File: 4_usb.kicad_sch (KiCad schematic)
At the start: 8 parts, among them J2 USB_C_Receptacle, U1 USBLC6-2SC6

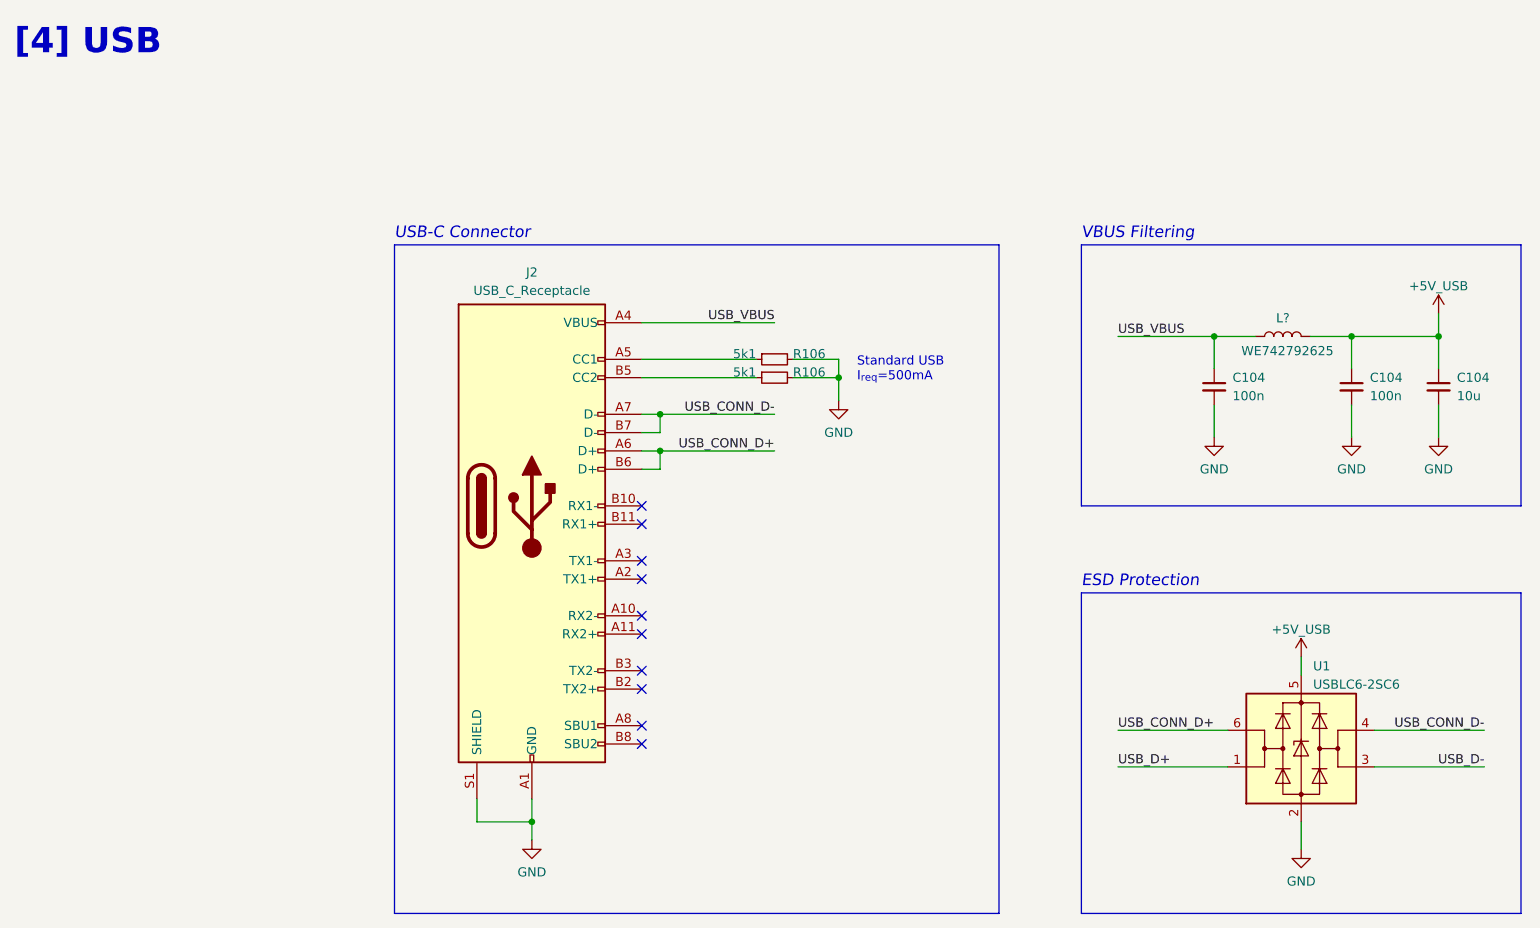
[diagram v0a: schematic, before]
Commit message: chore: updated links and footprints
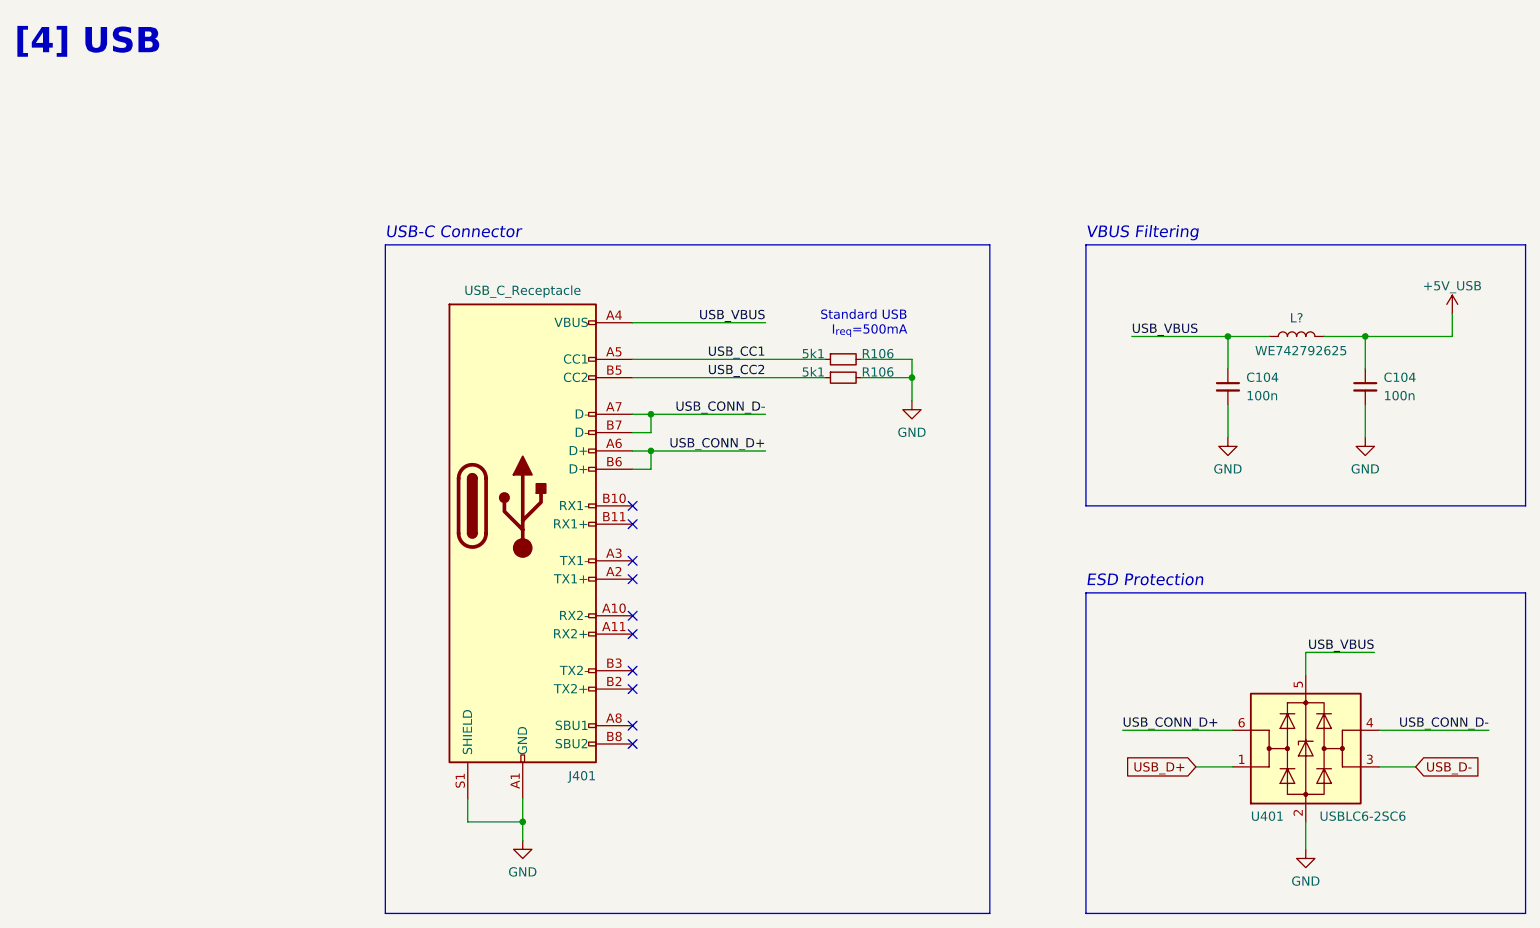
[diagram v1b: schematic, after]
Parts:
- removed C104: 10u, symbol Device:C_Small
- C104: footprint (none) -> Capacitor_SMD:C_0603_1608Metric_Pad1.08x0.95mm_HandSolder
- J401: renamed from J2; footprint (none) -> Connector_USB:USB_C_Receptacle_GCT_USB4105-xx-A_16P_TopMnt_Horizontal; Link (none) -> https://www.digikey.de/de/products/detail/gct/USB4105-GF-A/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
- L?: footprint (none) -> Inductor_SMD:L_0603_1608Metric_Pad1.05x0.95mm_HandSolder
- R106: footprint (none) -> Resistor_SMD:R_0402_1005Metric_Pad0.72x0.64mm_HandSolder
- U401: renamed from U1; Link (none) -> https://www.digikey.de/en/products/detail/stmicroelectronic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
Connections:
- net +5V: no longer U401.5 (VBUS)
- net USB_VBUS: now also U401.5 (VBUS)
- net USB_CC1: now reaches J401.A5 (CC1), R106.1
- net USB_CC2: now reaches J401.B5 (CC2), R106.1
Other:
- moved on the sheet: C104, J401, L?, R106, U401

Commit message: feat: LED routing, encoder interface, footprint updates
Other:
- title: USB [4] -> USB
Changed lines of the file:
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@@
   (paper "A4")
   (title_block
-    (title "USB [4]")
-    (date "2023-11-18")
+    (title "USB")
+    (date "2023-11-25")
     (rev "1.0")
   )

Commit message: feat: footprint assignment, circuit check and routing kickoff
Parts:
- C104: footprint Capacitor_SMD:C_0603_1608Metric_Pad1.08x0.95mm_HandSolder -> Capacitor_SMD:C_0402_1005Metric_Pad0.74x0.62mm_HandSolder
- L?: Link (none) -> https://www.digikey.de/en/products/detail/w%C3%BCrth-elektr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
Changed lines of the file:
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@@
   (title_block
     (title "USB")
-    (date "2023-11-25")
+    (date "2023-11-26")
     (rev "1.0")
   )
@@
       (effects (font (size 1.27 1.27)) hide)
     )
+    (property "Link" "https://www.digikey.de/en/products/detail/w%C3%BCrth-elektronik/742792625/4310426" (at 196.215 64.135 0)
+      (effects (font (size 1.27 1.27)) hide)
+    )
     (pin "1")
     (pin "2")
@@
       (effects (font (size 1.27 1.27)) (justify left))
     )
-    (property "Footprint" "Capacitor_SMD:C_0603_1608Metric_Pad1.08x0.95mm_HandSolder" (at 186.69 71.12 0)
+    (property "Footprint" "Capacitor_SMD:C_0402_1005Metric_Pad0.74x0.62mm_HandSolder" (at 186.69 71.12 0)
       (effects (font (size 1.27 1.27)) hide)
     )
@@
       (effects (font (size 1.27 1.27)) (justify left))
     )
-    (property "Footprint" "Capacitor_SMD:C_0603_1608Metric_Pad1.08x0.95mm_HandSolder" (at 205.74 71.12 0)
-      (effects (font (size 1.27 1.27)) hide)
-    )
+    (property "Footprint" "Capacitor_SMD:C_0402_1005Metric_Pad0.74x0.62mm_HandSolder" (at 205.74 71.12 0)
+      (effects (font (size 1.27 1.27)) hide)
+    )

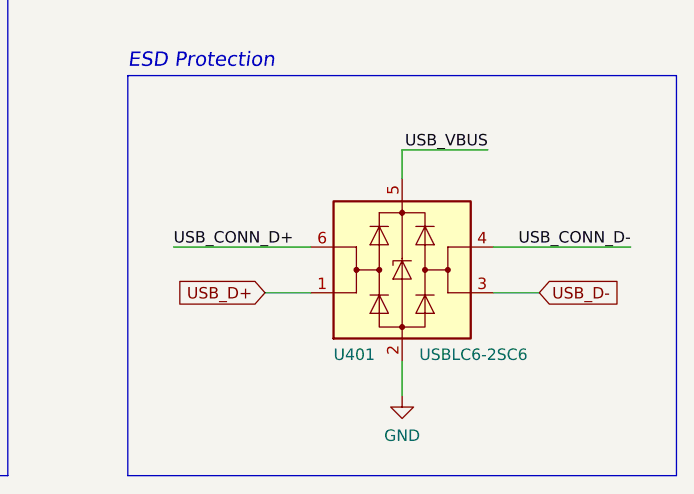
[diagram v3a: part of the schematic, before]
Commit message: feat: single phase, HSE, CAN routing and general layout
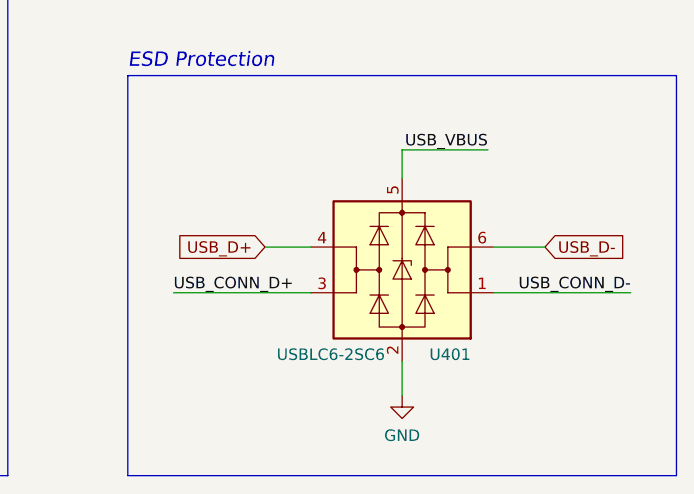
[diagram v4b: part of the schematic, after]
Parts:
- J401: footprint Connector_USB:USB_C_Receptacle_GCT_USB4105-xx-A_16P_TopMnt_Horizontal -> Connector_USB:USB_C_Receptacle_XKB_U262-16XN-4BVC11
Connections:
- net USB_CONN_D+: now also U401.3 (I/O2); no longer U401.6 (I/O1)
- net USB_CONN_D-: now also U401.1 (I/O1); no longer U401.4 (I/O2)
- net USB_D+: now also U401.4 (I/O2); no longer U401.1 (I/O1)
- net USB_D-: now also U401.6 (I/O1); no longer U401.3 (I/O2)
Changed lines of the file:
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@@
+    (stroke (width 0) (type default))
+  )
+  (wire (pts (xy 182.245 118.745) (xy 187.325 118.745))
     (stroke (width 0) (type default))
   )
@@
     (stroke (width 0) (type default))
   )
-  (wire (pts (xy 207.645 123.825) (xy 212.725 123.825))
+  (wire (pts (xy 207.645 123.825) (xy 222.885 123.825))
     (stroke (width 0) (type default))
   )
@@
     (stroke (width 0) (type default))
   )
+  (wire (pts (xy 207.645 118.745) (xy 213.36 118.745))
+    (stroke (width 0) (type default))
+  )
   (wire (pts (xy 104.14 74.93) (xy 106.68 74.93))
     (stroke (width 0) (type default))
@@
     (stroke (width 0) (type default))
   )
-  (wire (pts (xy 207.645 118.745) (xy 222.885 118.745))
-    (stroke (width 0) (type default))
-  )
   (wire (pts (xy 173.355 64.135) (xy 186.69 64.135))
     (stroke (width 0) (type default))
@@
     (stroke (width 0) (type default))
   )
-  (wire (pts (xy 172.085 118.745) (xy 187.325 118.745))
-    (stroke (width 0) (type default))
-  )
-  (wire (pts (xy 182.245 123.825) (xy 187.325 123.825))
+  (wire (pts (xy 172.085 123.825) (xy 187.325 123.825))
     (stroke (width 0) (type default))
   )
@@
     (effects (font (size 3.5 3.5) (thickness 0.8) bold) (justify left bottom))
   )
+  (label "USB_CONN_D-" (at 222.885 123.825 180) (fields_autoplaced)
+    (effects (font (size 1.27 1.27)) (justify right bottom))
+  )
   (label "USB_VBUS" (at 173.355 64.135 0) (fields_autoplaced)
     (effects (font (size 1.27 1.27)) (justify left bottom))
@@
     (effects (font (size 1.27 1.27)) (justify right bottom))
   )
-  (label "USB_CONN_D+" (at 172.085 118.745 0) (fields_autoplaced)
+  (label "USB_VBUS" (at 122.555 62.23 180) (fields_autoplaced)
+    (effects (font (size 1.27 1.27)) (justify right bottom))
+  )
+  (label "USB_CONN_D+" (at 172.085 123.825 0) (fields_autoplaced)
     (effects (font (size 1.27 1.27)) (justify left bottom))
   )
-  (label "USB_VBUS" (at 122.555 62.23 180) (fields_autoplaced)
-    (effects (font (size 1.27 1.27)) (justify right bottom))
-  )
   (label "USB_CC1" (at 122.555 67.31 180) (fields_autoplaced)
     (effects (font (size 1.27 1.27)) (justify right bottom))
   )
-  (label "USB_CONN_D-" (at 222.885 118.745 180) (fields_autoplaced)
-    (effects (font (size 1.27 1.27)) (justify right bottom))
-  )
   (label "USB_CONN_D-" (at 122.555 74.93 180) (fields_autoplaced)
     (effects (font (size 1.27 1.27)) (justify right bottom))
@@
     (effects (font (size 1.27 1.27)) (justify right bottom))
   )
-  (global_label "USB_D+" (shape input) (at 182.245 123.825 180) (fields_autoplaced)
+  (global_label "USB_D-" (shape input) (at 213.36 118.745 0) (fields_autoplaced)
+    (effects (font (size 1.27 1.27)) (justify left))
+    (property "Intersheetrefs" "${INTERSHEET_REFS}" (at 223.8858 118.745 0)
+      (effects (font (size 1.27 1.27)) (justify left) hide)
+    )
+  )
+  (global_label "USB_D+" (shape input) (at 182.245 118.745 180) (fields_autoplaced)
     (effects (font (size 1.27 1.27)) (justify right))
-    (property "Intersheetrefs" "${INTERSHEET_REFS}" (at 171.7192 123.825 0)
+    (property "Intersheetrefs" "${INTERSHEET_REFS}" (at 171.7192 118.745 0)
       (effects (font (size 1.27 1.27)) (justify right) hide)
     )
   )
-  (global_label "USB_D-" (shape input) (at 212.725 123.825 0) (fields_autoplaced)
-    (effects (font (size 1.27 1.27)) (justify left))
-    (property "Intersheetrefs" "${INTERSHEET_REFS}" (at 223.2508 123.825 0)
-      (effects (font (size 1.27 1.27)) (justify left) hide)
-    )
-  )
   (symbol (lib_id "Connector:USB_C_Receptacle") (at 88.9 87.63 0) (unit 1)
     (in_bom yes) (on_board yes) (dnp no)
@@
       (effects (font (size 1.27 1.27)))
     )
-    (property "Footprint" "Connector_USB:USB_C_Receptacle_GCT_USB4105-xx-A_16P_TopMnt_Horizontal" (at 92.71 87.63 0)
+    (property "Footprint" "Connector_USB:USB_C_Receptacle_XKB_U262-16XN-4BVC11" (at 92.71 87.63 0)
       (effects (font (size 1.27 1.27)) hide)
     )
@@
     )
   )
-  (symbol (lib_id "Power_Protection:USBLC6-2SC6") (at 197.485 121.285 0) (unit 1)
-    (in_bom yes) (on_board yes) (dnp no)
-    (property "Reference" "U401" (at 189.865 131.445 0)
+  (symbol (lib_id "Power_Protection:USBLC6-2SC6") (at 197.485 121.285 0) (mirror y) (unit 1)
+    (in_bom yes) (on_board yes) (dnp no)
+    (property "Reference" "U401" (at 205.105 131.445 0)
       (effects (font (size 1.27 1.27)) (justify left bottom))
     )
-    (property "Value" "USBLC6-2SC6" (at 199.39 131.445 0)
+    (property "Value" "USBLC6-2SC6" (at 195.58 131.445 0)
       (effects (font (size 1.27 1.27)) (justify left bottom))
     )
@@
       (effects (font (size 1.27 1.27)) hide)
     )
-    (property "Datasheet" "https://www.st.com/resource/en/datasheet/usblc6-2.pdf" (at 202.565 112.395 0)
-      (effects (font (size 1.27 1.27)) hide)
-    )
+    (property "Datasheet" "https://www.st.com/resource/en/datasheet/usblc6-2.pdf" (at 192.405 112.395 0)
+      (effects (font (size 1.27 1.27)) hide)
+    )

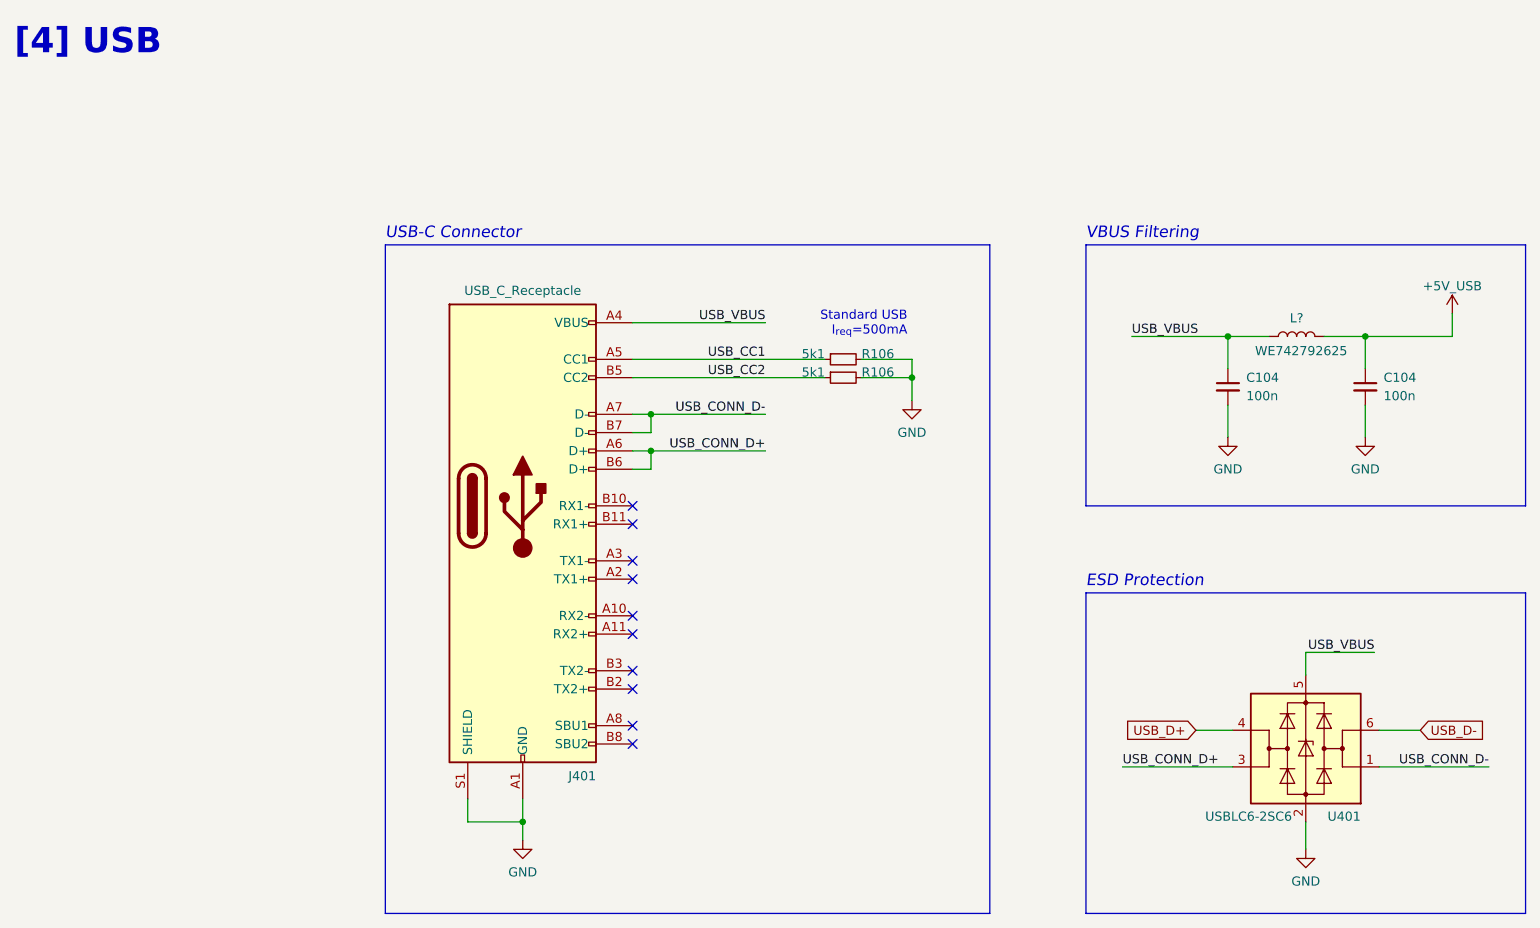
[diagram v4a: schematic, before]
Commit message: feat: major circuit rework, style update and addition of a few extra subcomponents
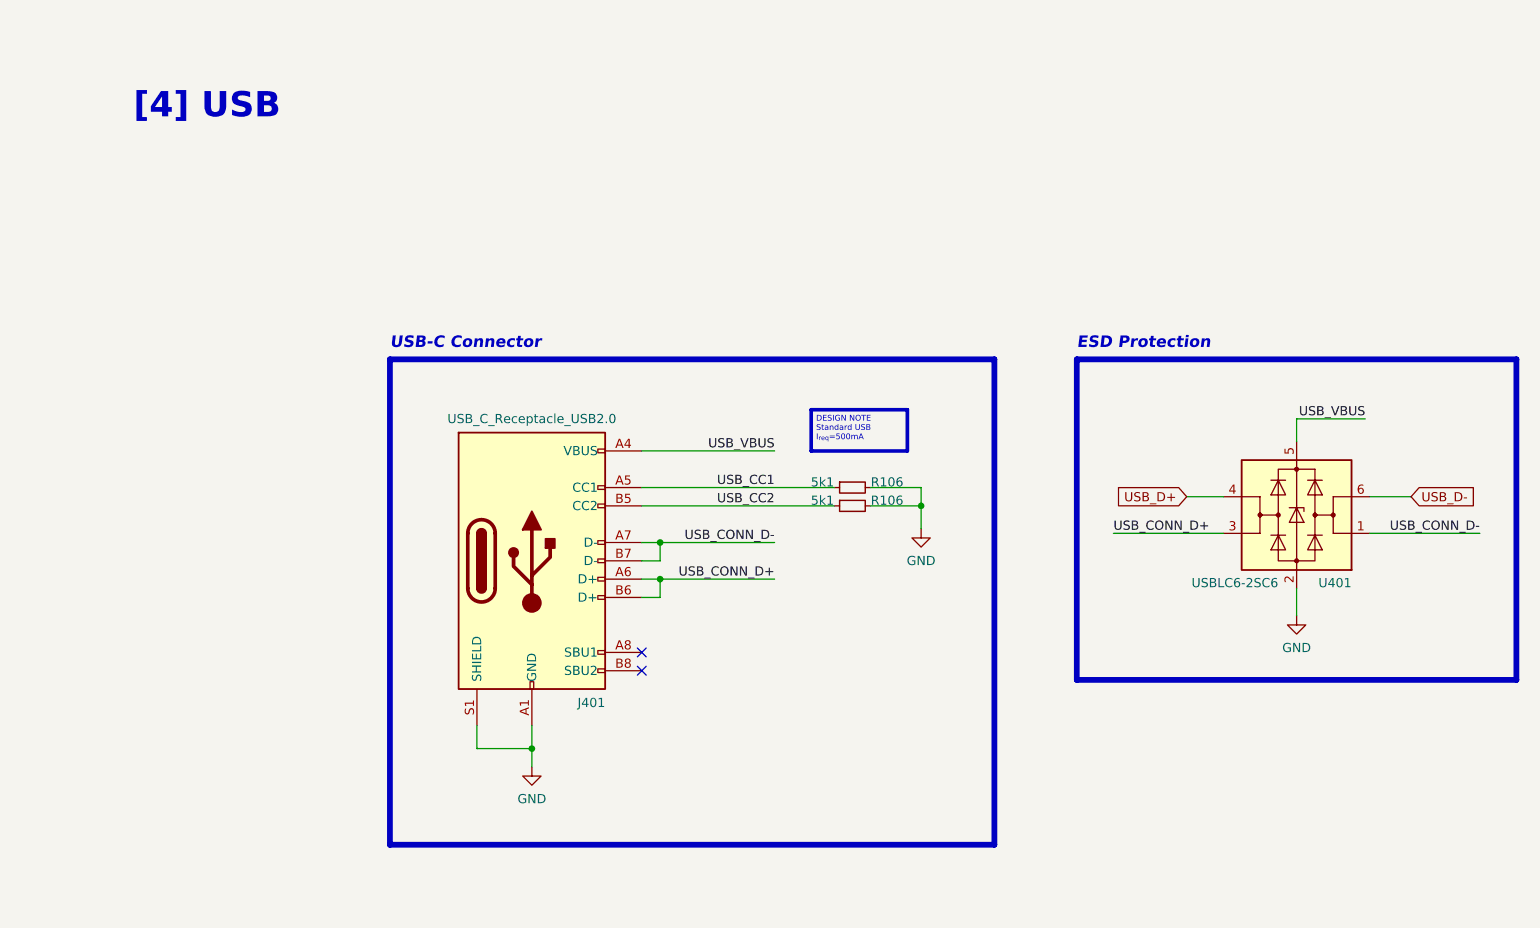
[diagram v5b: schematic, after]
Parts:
- removed C104 (x2): 100n, Capacitor_SMD:C_0402_1005Metric_Pad0.74x0.62mm_HandSolder, symbol Device:C_Small
- removed J401: USB_C_Receptacle, Connector_USB:USB_C_Receptacle_XKB_U262-16XN-4BVC11, symbol Connector:USB_C_Receptacle
- removed L?: WE742792625, Inductor_SMD:L_0603_1608Metric_Pad1.05x0.95mm_HandSolder, symbol Device:L
- added J401: USB_C_Receptacle_USB2.0, Connector_USB:USB_C_Receptacle_XKB_U262-16XN-4BVC11, symbol Connector:USB_C_Receptacle_USB2.0
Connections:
- net GND: now also J401.A1 (GND), J401.A12 (GND), J401.B1 (GND), J401.B12 (GND), J401.S1 (SHIELD)
- net USB_CC1: now also J401.A5 (CC1)
- net USB_CC2: now also J401.B5 (CC2)
- net USB_CONN_D+: now also J401.A6 (D+), J401.B6 (D+)
- net USB_CONN_D-: now also J401.A7 (D-), J401.B7 (D-)
- net USB_VBUS: now also J401.A4 (VBUS), J401.A9 (VBUS), J401.B4 (VBUS), J401.B9 (VBUS)
- no-connect marks 10 -> 2
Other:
- note removed: "Standard USB I_{req}=500mA"
- note removed: "VBUS Filtering"
- moved on the sheet: R106, U401
